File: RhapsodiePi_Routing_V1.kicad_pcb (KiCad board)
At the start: 6 copper layers, 85.2 x 56.1 mm, 261 parts, among them J1 Micro_SD_Card_Det, J2 Conn_Coaxial, J3 Conn_02x05_Odd_Even, J4 USB_A_Stacked, J5 USB_A_Stacked, J7 RJ45_HR913550A, J8 HDMI_A, J9 AudioJack4, P1 USB_C_Plug, U1 IMX6UL, U10 FE2.1, U11 RTL8201F, U12 TFP410PAP, U13 LM4871, U14 LM4871, U15 TPS65185RGZR, U2 MT3420C-mt3420c, U3 MT3420C-mt3420c, U4 MT3420C-mt3420c, U5 MKDN0xxxCL, U6 MT41K256M16TW, U7 MT41K256M16TW, U8 X1000, U9 AP6212, Y1 12MHz, Y2 24MHz, Y3 32.768kHz

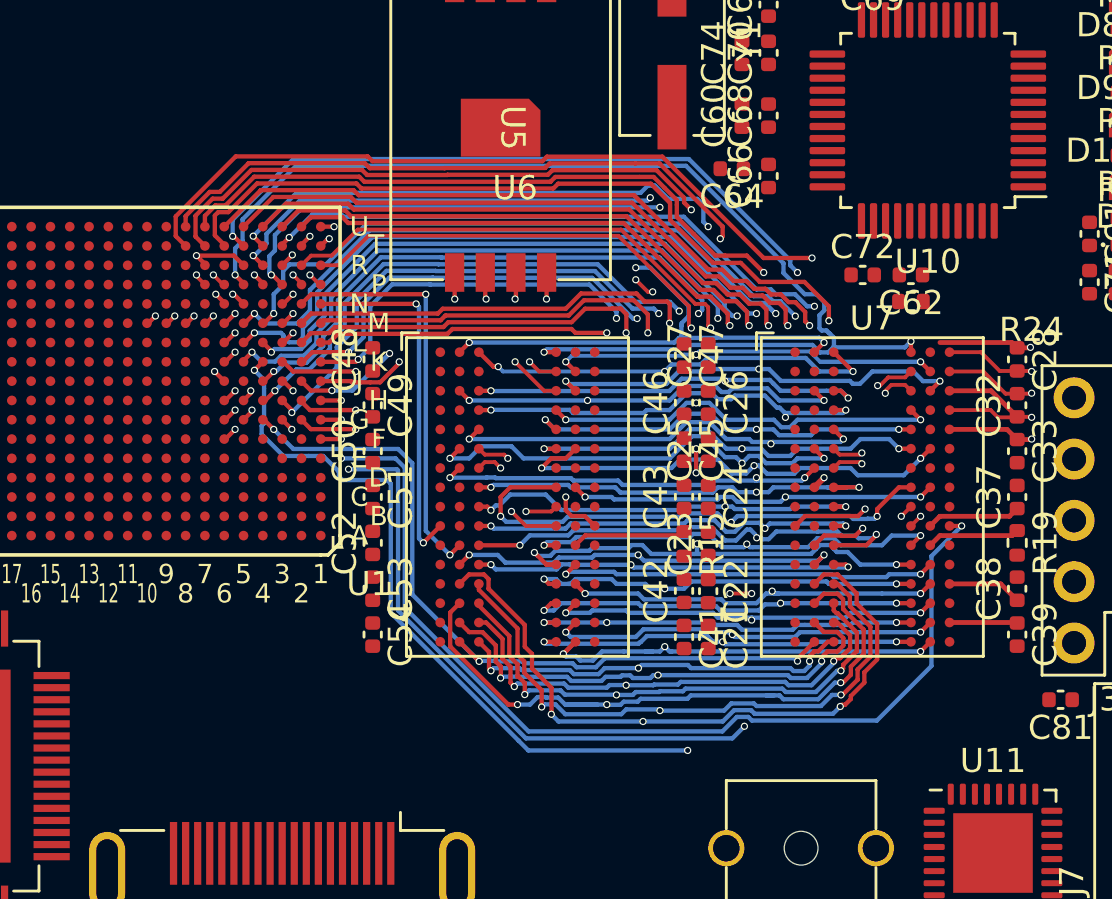
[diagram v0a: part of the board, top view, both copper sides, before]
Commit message: update DDR
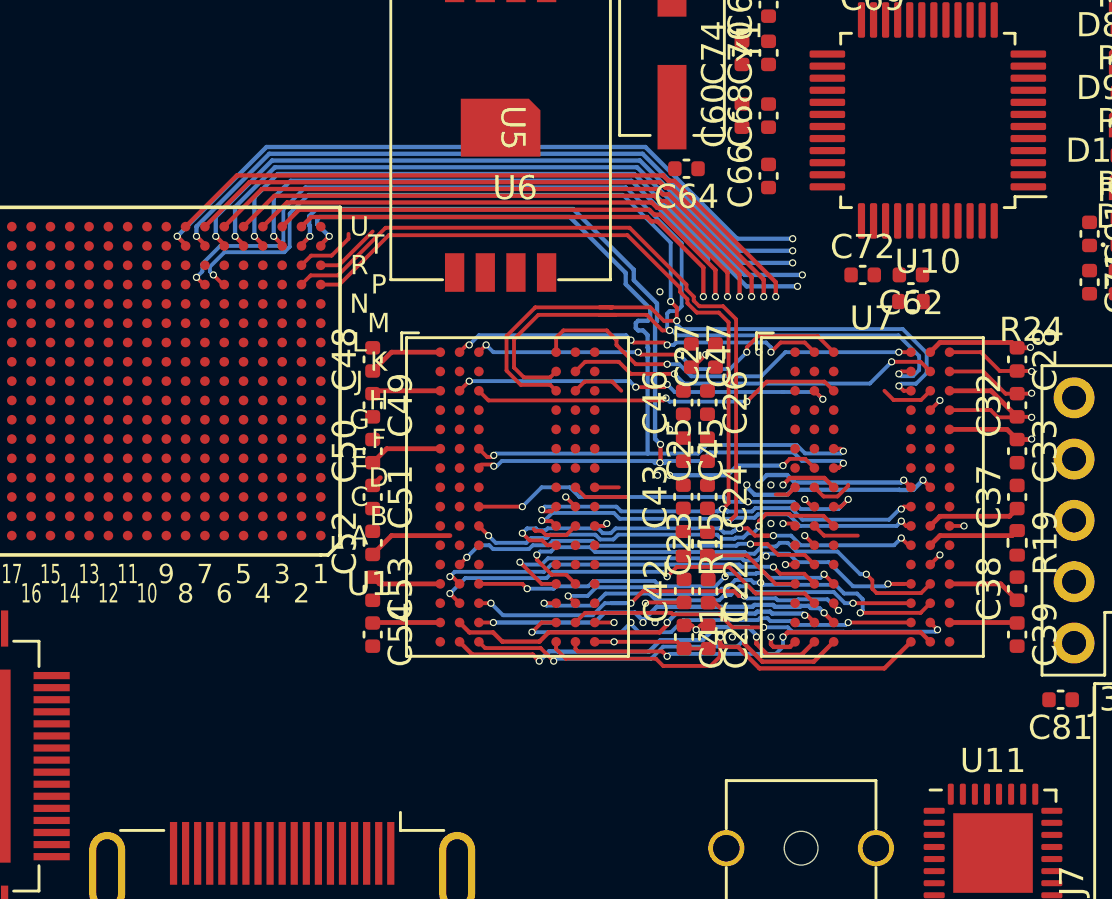
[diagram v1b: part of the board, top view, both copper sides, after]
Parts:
- moved C64 1.88 mm to (133.1, 80.6)
- moved C27 0.30 mm to (134.3, 88.3)
- moved C47 0.30 mm to (133.3, 88.3)
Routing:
- net /Memory/MMDC_~{WE}: track 64.3 -> 0.00 mm, vias 4 -> 0
- net /Memory/MMDC_A0: track 69.4 -> 15.5 mm, vias 5 -> 3
- net /Memory/MMDC_~{CAS}: track 63.4 -> 16.2 mm, vias 5 -> 2
- net /Memory/MMDC_A3: track 62.9 -> 16.2 mm, vias 4 -> 2
- net /Memory/MMDC_CKE1: track 45.3 -> 0.60 mm, vias 3 -> 1
- net /Memory/MMDC_~{CS1}: track 44.3 -> 0.57 mm, vias 4 -> 1
- net /Memory/MMDC_BA2: track 43.5 -> 0.00 mm, vias 5 -> 0
- net /Memory/MMDC_ODT1: track 43.6 -> 0.54 mm, vias 2 -> 1
- net /Memory/MMDC_A7: track 57.7 -> 15.8 mm, vias 5 -> 2
- net /Memory/MMDC_A8: track 54.9 -> 15.9 mm, vias 5 -> 2
- net /Memory/MMDC_A5: track 55.2 -> 16.9 mm, vias 4 -> 2
- net /Memory/MMDC_A2: track 53.4 -> 16.9 mm, vias 5 -> 4
- net /Memory/MMDC_A13: track 52.6 -> 16.4 mm, vias 5 -> 2
- net /Memory/MMDC_A12: track 55.7 -> 19.7 mm, vias 5 -> 3
- net /Memory/MMDC_A10: track 54.8 -> 19.0 mm, vias 5 -> 4
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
